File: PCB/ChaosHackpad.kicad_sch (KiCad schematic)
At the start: 22 parts, among them SW1 RotaryEncoder_Switch, SW2 SW_Push_45deg, SW3 SW_Push_45deg, SW4 SW_Push_45deg, SW5 SW_Push_45deg, SW6 SW_Push_45deg, SW7 SW_Push_45deg, SW8 SW_Push_45deg, U1 XIAO-RP2040-DIP

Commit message: added 3d models
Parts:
- SW2, SW3, SW4, SW5, SW6, SW7, SW8: footprint Button_Switch_Keyboard:SW_Cherry_MX_1.00u_PCB -> CustomSwitches:SW_Cherry_MX_1.00u_PCB
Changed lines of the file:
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@@
 			)
 		)
-		(property "Footprint" "Button_Switch_Keyboard:SW_Cherry_MX_1.00u_PCB"
+		(property "Footprint" "CustomSwitches:SW_Cherry_MX_1.00u_PCB"
 			(at 38.1 71.12 0)
 			(effects
@@
 			)
 		)
-		(property "Footprint" "Button_Switch_Keyboard:SW_Cherry_MX_1.00u_PCB"
+		(property "Footprint" "CustomSwitches:SW_Cherry_MX_1.00u_PCB"
 			(at 101.6 44.45 0)
 			(effects
@@
 			)
 		)
-		(property "Footprint" "Button_Switch_Keyboard:SW_Cherry_MX_1.00u_PCB"
+		(property "Footprint" "CustomSwitches:SW_Cherry_MX_1.00u_PCB"
 			(at 101.6 71.12 0)
 			(effects
@@
 			)
 		)
-		(property "Footprint" "Button_Switch_Keyboard:SW_Cherry_MX_1.00u_PCB"
+		(property "Footprint" "CustomSwitches:SW_Cherry_MX_1.00u_PCB"
 			(at 38.1 44.45 0)
 			(effects
@@
 			)
 		)
-		(property "Footprint" "Button_Switch_Keyboard:SW_Cherry_MX_1.00u_PCB"
+		(property "Footprint" "CustomSwitches:SW_Cherry_MX_1.00u_PCB"
 			(at 69.85 44.45 0)
 			(effects
@@
 			)
 		)
-		(property "Footprint" "Button_Switch_Keyboard:SW_Cherry_MX_1.00u_PCB"
+		(property "Footprint" "CustomSwitches:SW_Cherry_MX_1.00u_PCB"
 			(at 133.35 44.45 0)
 			(effects
@@
 			)
 		)
-		(property "Footprint" "Button_Switch_Keyboard:SW_Cherry_MX_1.00u_PCB"
+		(property "Footprint" "CustomSwitches:SW_Cherry_MX_1.00u_PCB"
 			(at 69.85 71.12 0)
 			(effects

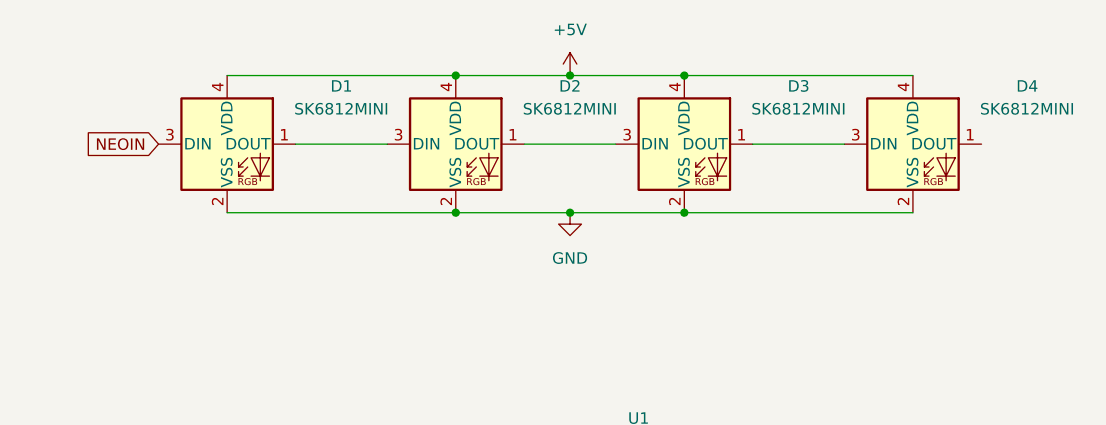
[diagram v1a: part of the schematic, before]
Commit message: rerouted and redesigned PCB, fixed broken footprints/symbols
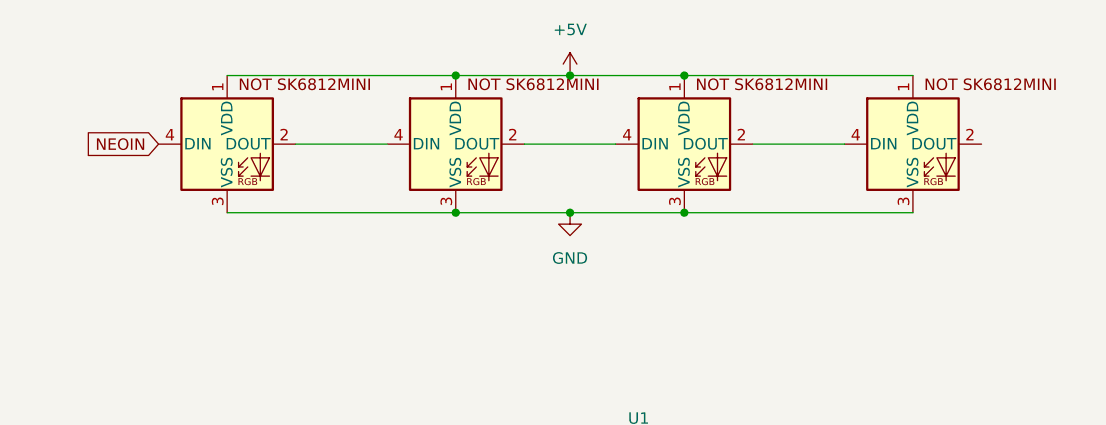
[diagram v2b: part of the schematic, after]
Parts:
- D1, D2, D3, D4: footprint LED_SMD:LED_SK6812MINI_PLCC4_3.5x3.5mm_P1.75mm -> SK6812MINI-E:SK6812MINI-E_fixed; symbol LED:SK6812MINI -> SK6812MINI-E:SK6812MINI-E
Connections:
- net +5V: now also D1.1 (VDD), D2.1 (VDD), D3.1 (VDD), D4.1 (VDD); no longer D1.4 (VDD), D2.4 (VDD), D3.4 (VDD), D4.4 (VDD)
- net GND: now also D1.3 (VSS), D2.3 (VSS), D3.3 (VSS), D4.3 (VSS); no longer D1.2 (VSS), D2.2 (VSS), D3.2 (VSS), D4.2 (VSS)
- net NEOIN: now also D1.4 (DIN); no longer D1.3 (DIN)
- new net: D1.2 (DOUT), D2.4 (DIN)
- new net: D3.2 (DOUT), D4.4 (DIN)
- new net: D2.2 (DOUT), D3.4 (DIN)
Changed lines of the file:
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@@
 	)
 	(symbol
-		(lib_id "LED:SK6812MINI")
+		(lib_id "SK6812MINI-E:SK6812MINI-E")
 		(at 181.61 35.56 0)
 		(unit 1)
@@
 		(fields_autoplaced yes)
 		(property "Reference" "D1"
-			(at 194.31 29.1398 0)
-			(effects
-				(font
-					(size 1.27 1.27)
-				)
+			(at 205.74 29.1398 0)
+			(effects
+				(font
+					(size 1.27 1.27)
+				)
+				(hide yes)
 			)
 		)
 		(property "Value" "SK6812MINI"
-			(at 194.31 31.6798 0)
-			(effects
-				(font
-					(size 1.27 1.27)
-				)
-			)
-		)
-		(property "Footprint" "LED_SMD:LED_SK6812MINI_PLCC4_3.5x3.5mm_P1.75mm"
+			(at 205.74 31.6798 0)
+			(effects
+				(font
+					(size 1.27 1.27)
+				)
+				(hide yes)
+			)
+		)
+		(property "Footprint" "SK6812MINI-E:SK6812MINI-E_fixed"
 			(at 182.88 43.18 0)
 			(effects
@@
 			)
 		)
-		(property "Datasheet" "https://cdn-shop.adafruit.com/product-files/2686/SK6812MINI_REV.01-1-2.pdf"
+		(property "Datasheet" "https://cdn-shop.adafruit.com/product-files/4960/4960_SK6812MINI-E_REV02_EN.pdf"
 			(at 184.15 45.085 0)
 			(effects
@@
 	)
 	(symbol
-		(lib_id "LED:SK6812MINI")
+		(lib_id "SK6812MINI-E:SK6812MINI-E")
 		(at 232.41 35.56 0)
 		(unit 1)
@@
 		(fields_autoplaced yes)
 		(property "Reference" "D3"
-			(at 245.11 29.1398 0)
-			(effects
-				(font
-					(size 1.27 1.27)
-				)
+			(at 256.54 29.1398 0)
+			(effects
+				(font
+					(size 1.27 1.27)
+				)
+				(hide yes)
 			)
 		)
 		(property "Value" "SK6812MINI"
-			(at 245.11 31.6798 0)
-			(effects
-				(font
-					(size 1.27 1.27)
-				)
-			)
-		)
-		(property "Footprint" "LED_SMD:LED_SK6812MINI_PLCC4_3.5x3.5mm_P1.75mm"
+			(at 256.54 31.6798 0)
+			(effects
+				(font
+					(size 1.27 1.27)
+				)
+				(hide yes)
+			)
+		)
+		(property "Footprint" "SK6812MINI-E:SK6812MINI-E_fixed"
 			(at 233.68 43.18 0)
 			(effects
@@
 			)
 		)
-		(property "Datasheet" "https://cdn-shop.adafruit.com/product-files/2686/SK6812MINI_REV.01-1-2.pdf"
+		(property "Datasheet" "https://cdn-shop.adafruit.com/product-files/4960/4960_SK6812MINI-E_REV02_EN.pdf"
 			(at 234.95 45.085 0)
 			(effects
@@
 	)
 	(symbol
-		(lib_id "LED:SK6812MINI")
+		(lib_id "SK6812MINI-E:SK6812MINI-E")
 		(at 257.81 35.56 0)
 		(unit 1)
@@
 		(fields_autoplaced yes)
 		(property "Reference" "D4"
-			(at 270.51 29.1398 0)
-			(effects
-				(font
-					(size 1.27 1.27)
-				)
+			(at 281.94 29.1398 0)
+			(effects
+				(font
+					(size 1.27 1.27)
+				)
+				(hide yes)
 			)
 		)
 		(property "Value" "SK6812MINI"
-			(at 270.51 31.6798 0)
-			(effects
-				(font
-					(size 1.27 1.27)
-				)
-			)
-		)
-		(property "Footprint" "LED_SMD:LED_SK6812MINI_PLCC4_3.5x3.5mm_P1.75mm"
+			(at 281.94 31.6798 0)
+			(effects
+				(font
+					(size 1.27 1.27)
+				)
+				(hide yes)
+			)
+		)
+		(property "Footprint" "SK6812MINI-E:SK6812MINI-E_fixed"
 			(at 259.08 43.18 0)
 			(effects
@@
 			)
 		)
-		(property "Datasheet" "https://cdn-shop.adafruit.com/product-files/2686/SK6812MINI_REV.01-1-2.pdf"
+		(property "Datasheet" "https://cdn-shop.adafruit.com/product-files/4960/4960_SK6812MINI-E_REV02_EN.pdf"
 			(at 260.35 45.085 0)
 			(effects
@@
 	)
 	(symbol
-		(lib_id "LED:SK6812MINI")
+		(lib_id "SK6812MINI-E:SK6812MINI-E")
 		(at 207.01 35.56 0)
 		(unit 1)
@@
 		(fields_autoplaced yes)
 		(property "Reference" "D2"
-			(at 219.71 29.1398 0)
-			(effects
-				(font
-					(size 1.27 1.27)
-				)
+			(at 231.14 29.1398 0)
+			(effects
+				(font
+					(size 1.27 1.27)
+				)
+				(hide yes)
 			)
 		)
 		(property "Value" "SK6812MINI"
-			(at 219.71 31.6798 0)
-			(effects
-				(font
-					(size 1.27 1.27)
-				)
-			)
-		)
-		(property "Footprint" "LED_SMD:LED_SK6812MINI_PLCC4_3.5x3.5mm_P1.75mm"
+			(at 231.14 31.6798 0)
+			(effects
+				(font
+					(size 1.27 1.27)
+				)
+				(hide yes)
+			)
+		)
+		(property "Footprint" "SK6812MINI-E:SK6812MINI-E_fixed"
 			(at 208.28 43.18 0)
 			(effects
@@
 			)
 		)
-		(property "Datasheet" "https://cdn-shop.adafruit.com/product-files/2686/SK6812MINI_REV.01-1-2.pdf"
+		(property "Datasheet" "https://cdn-shop.adafruit.com/product-files/4960/4960_SK6812MINI-E_REV02_EN.pdf"
 			(at 209.55 45.085 0)
 			(effects
